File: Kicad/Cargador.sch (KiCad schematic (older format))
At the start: 7 parts, among them P3 MICRO_USB_B, U4 MCP73831

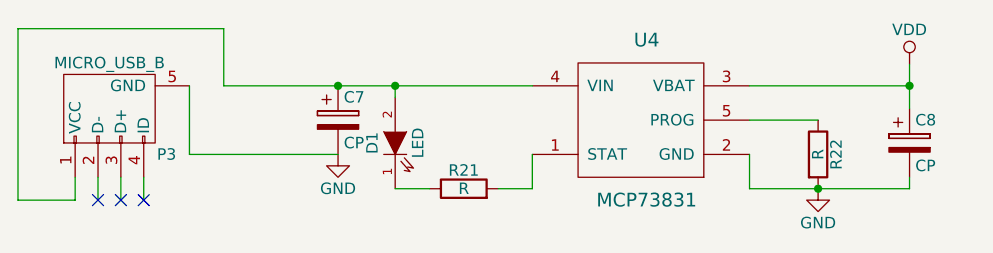
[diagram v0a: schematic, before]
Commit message: Se cambia la datasheet del usb. Se agrega los step y wrl del nrf.
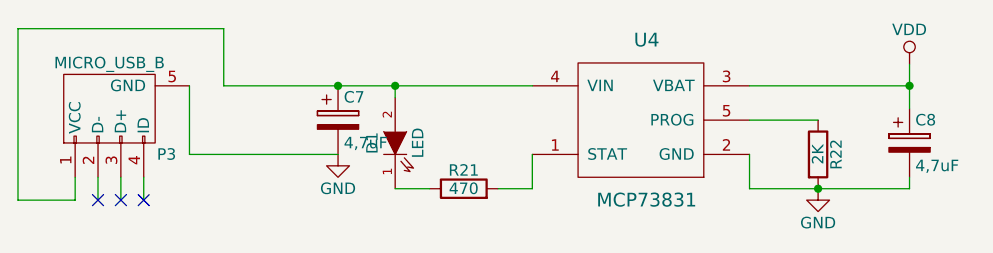
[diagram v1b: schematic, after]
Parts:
- C7, C8: value CP -> 4,7uF
- R21: value R -> 470
- R22: value R -> 2K
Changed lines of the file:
@@
 P 6400 3350
 F 0 "C8" H 6425 3450 50  0000 L CNN
-F 1 "CP" H 6425 3250 50  0000 L CNN
+F 1 "4,7uF" H 6425 3250 50  0000 L CNN
 F 2 "EMG:C_0603" H 6438 3200 50  0001 C CNN
 F 3 "" H 6400 3350 50  0000 C CNN
@@
 P 3900 3250
 F 0 "C7" H 3925 3350 50  0000 L CNN
-F 1 "CP" H 3925 3150 50  0000 L CNN
+F 1 "4,7uF" H 3925 3150 50  0000 L CNN
 F 2 "EMG:C_0603" H 3938 3100 50  0001 C CNN
 F 3 "" H 3900 3250 50  0000 C CNN
@@
 P 6000 3400
 F 0 "R22" V 6080 3400 50  0000 C CNN
-F 1 "R" V 6000 3400 50  0000 C CNN
+F 1 "2K" V 6000 3400 50  0000 C CNN
 F 2 "EMG:R_0603" V 5930 3400 50  0001 C CNN
 F 3 "" H 6000 3400 50  0000 C CNN
@@
 P 4450 3550
 F 0 "R21" V 4530 3550 50  0000 C CNN
-F 1 "R" V 4450 3550 50  0000 C CNN
+F 1 "470" V 4450 3550 50  0000 C CNN
 F 2 "EMG:R_0603" V 4380 3550 50  0001 C CNN
 F 3 "" H 4450 3550 50  0000 C CNN
